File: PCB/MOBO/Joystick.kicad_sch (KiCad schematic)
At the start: 0 parts

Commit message: added full atmega circuit and programming interface
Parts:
- added C4, C5: 22pF, symbol Device:C
- added C6: 100nF, symbol Device:C
- added J107: DTR, TestPoint:TestPoint_Pad_1.5x1.5mm, symbol Connector:Conn_01x01_Male
- added J107: SCK, TestPoint:TestPoint_Pad_1.5x1.5mm, symbol Connector:Conn_01x01_Male
- added J107: TXD, TestPoint:TestPoint_Pad_1.5x1.5mm, symbol Connector:Conn_01x01_Male
- added J107: RXD, TestPoint:TestPoint_Pad_1.5x1.5mm, symbol Connector:Conn_01x01_Male
- added J107: MOSI, TestPoint:TestPoint_Pad_1.5x1.5mm, symbol Connector:Conn_01x01_Male
- added J107: MISO, TestPoint:TestPoint_Pad_1.5x1.5mm, symbol Connector:Conn_01x01_Male
- added R15: 10k, symbol Device:R
- added SW2: Reset_Button, Button_Switch_THT:SW_PUSH_6mm, symbol PCM_SL_Devices:Push_Button
- added U4: ATmega328PB-M, Package_DFN_QFN:QFN-32-1EP_5x5mm_P0.5mm_EP3.1x3.1mm, symbol MCU_Microchip_ATmega:ATmega328PB-M
- added Y1: 116MHz, symbol Device:Crystal
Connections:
- new net: C5.2, U4.8 (XTAL2/PB7), Y1.2
- new net: C6.2, J107.1 (Pin_1)
- new net: C4.1, U4.7 (XTAL1/PB6), Y1.1
- new net 5V_IN: R15.2, U4.18 (AVCC), U4.4 (VCC)
- new net BTN_A: U4.12 (PB0)
- new net BTN_B: U4.13 (PB1)
- new net BTN_DWN: U4.24 (PC1)
- new net BTN_LEFT: U4.25 (PC2)
- new net BTN_LS: U4.14 (PB2)
- new net BTN_RIGHT: U4.26 (PC3)
- new net BTN_RS: U4.32 (PD2)
- new net BTN_UP: U4.23 (PC0)
- new net GND: C4.2, C5.1, SW2.2, U4.21 (GND), U4.33 (GND), U4.5 (GND)
- new net MISO: J107.1 (Pin_1), U4.16 (PB4)
- new net MOSI: J107.1 (Pin_1), U4.15 (PB3)
- new net RESET: C6.1, R15.1, SW2.1, U4.29 (~{RESET}/PC6)
- new net RXD: J107.1 (Pin_1), U4.30 (PD0)
- new net SCK: J107.1 (Pin_1), U4.17 (PB5)
- new net SCL: U4.28 (PC5)
- new net SDA: U4.27 (PC4)
- new net TXD: J107.1 (Pin_1), U4.31 (PD1)
- no-connect marks 0 -> 10

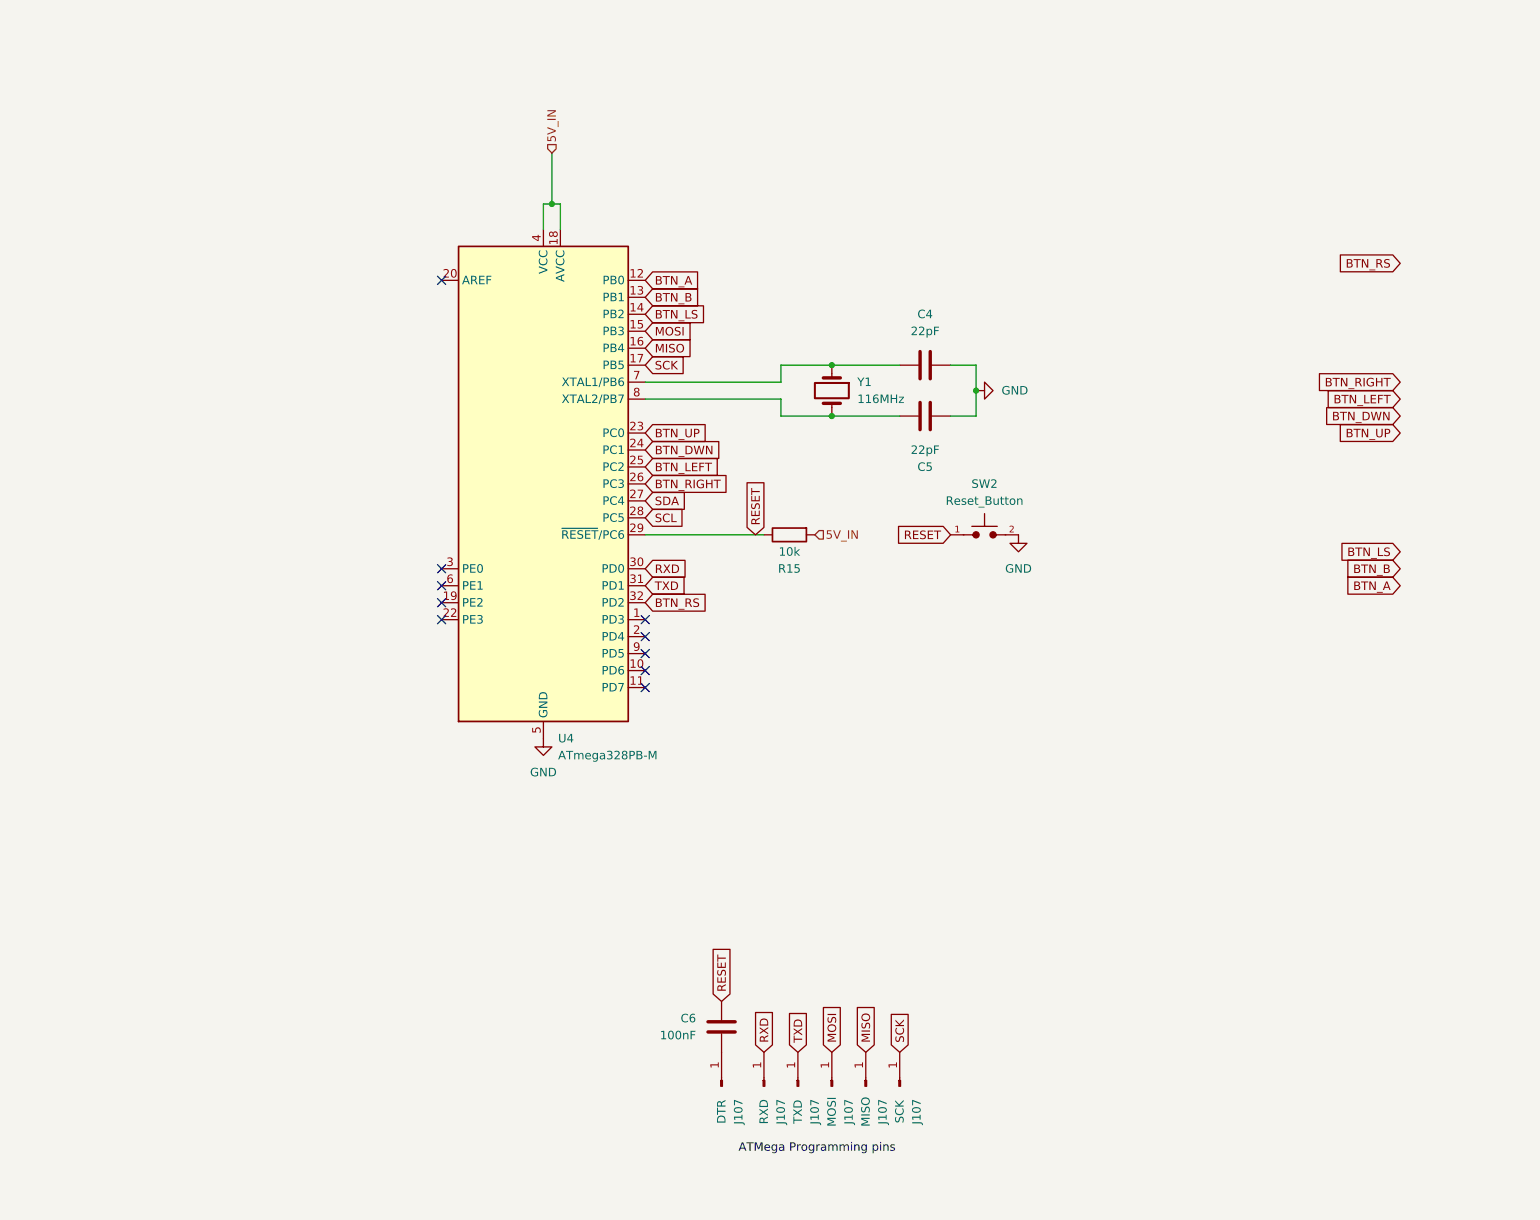
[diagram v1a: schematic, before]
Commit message: added all joystick buttons
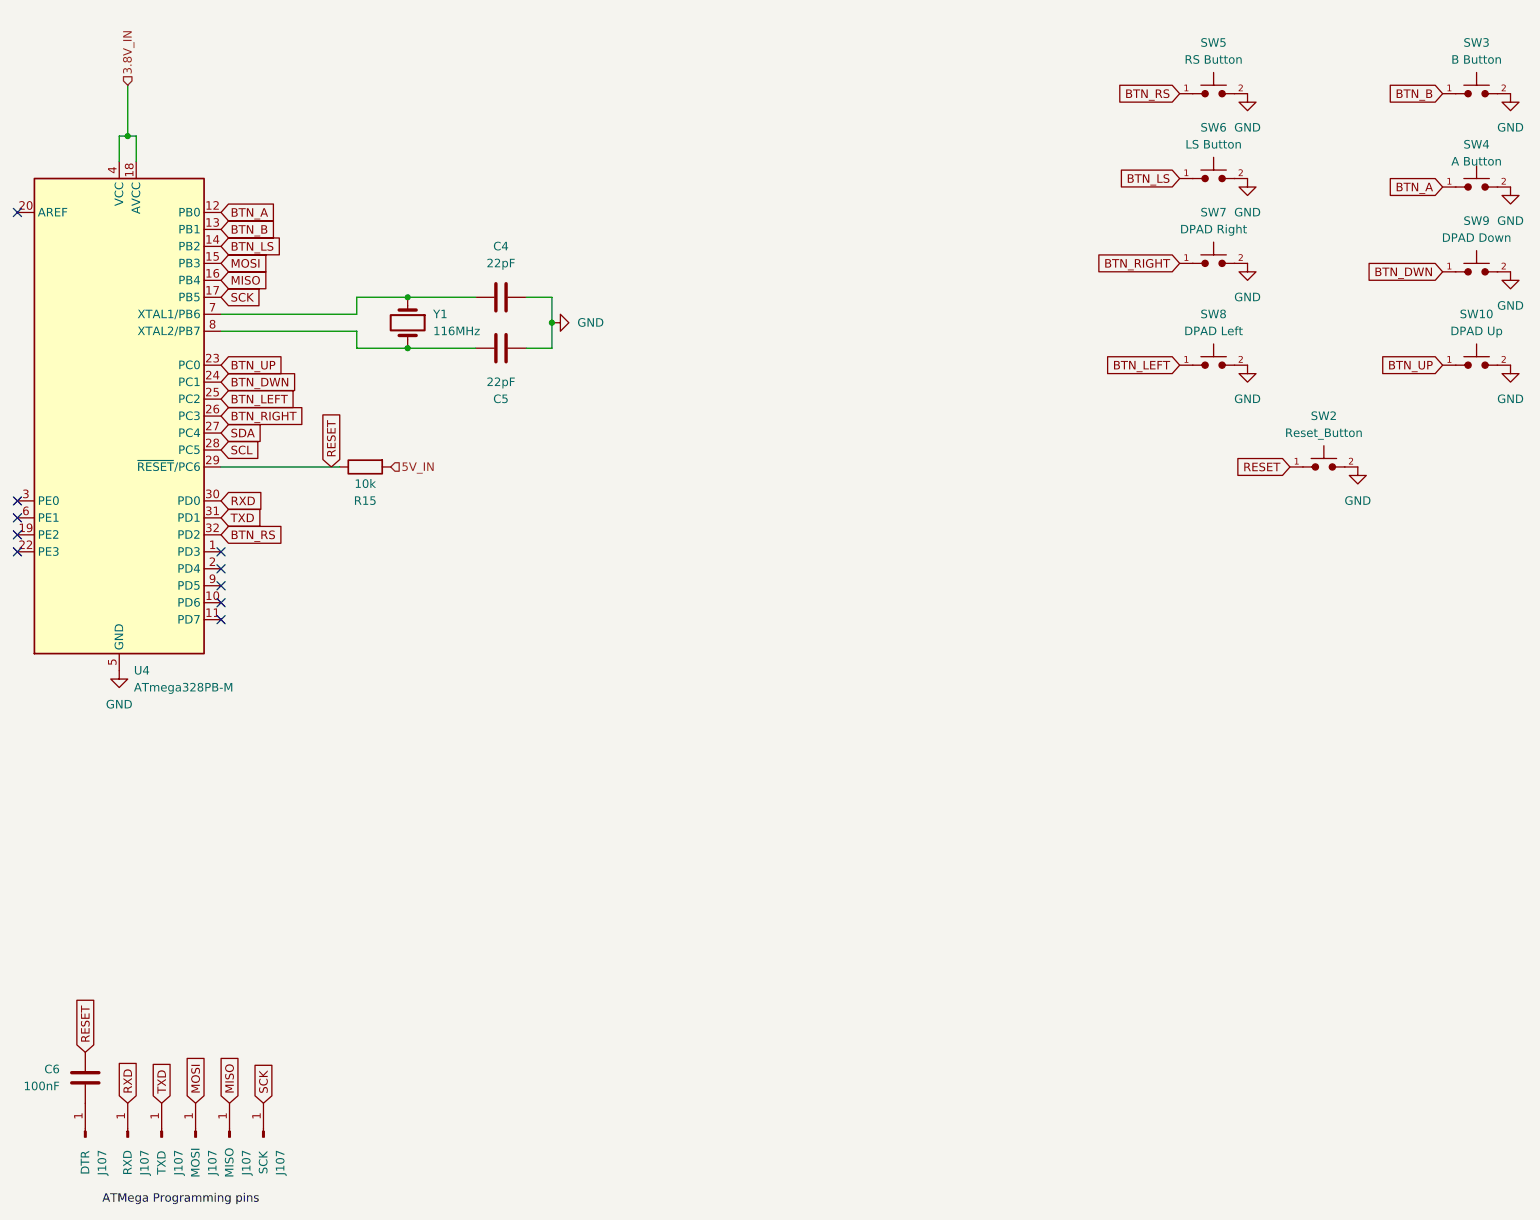
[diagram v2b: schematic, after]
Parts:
- added SW10: DPAD Up, Button_Switch_THT:SW_PUSH_6mm, symbol PCM_SL_Devices:Push_Button
- added SW3: B Button, Button_Switch_THT:SW_PUSH_6mm, symbol PCM_SL_Devices:Push_Button
- added SW4: A Button, Button_Switch_THT:SW_PUSH_6mm, symbol PCM_SL_Devices:Push_Button
- added SW5: RS Button, Button_Switch_THT:SW_PUSH_6mm, symbol PCM_SL_Devices:Push_Button
- added SW6: LS Button, Button_Switch_THT:SW_PUSH_6mm, symbol PCM_SL_Devices:Push_Button
- added SW7: DPAD Right, Button_Switch_THT:SW_PUSH_6mm, symbol PCM_SL_Devices:Push_Button
- added SW8: DPAD Left, Button_Switch_THT:SW_PUSH_6mm, symbol PCM_SL_Devices:Push_Button
- added SW9: DPAD Down, Button_Switch_THT:SW_PUSH_6mm, symbol PCM_SL_Devices:Push_Button
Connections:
- net 5V_IN: no longer U4.18 (AVCC), U4.4 (VCC)
- net BTN_A: now also SW4.1
- net BTN_B: now also SW3.1
- net BTN_DWN: now also SW9.1
- net BTN_LEFT: now also SW8.1
- net BTN_LS: now also SW6.1
- net BTN_RIGHT: now also SW7.1
- net BTN_RS: now also SW5.1
- net BTN_UP: now also SW10.1
- net GND: now also SW10.2, SW3.2, SW4.2, SW5.2, SW6.2, SW7.2, SW8.2, SW9.2
- new net 3.8V_IN: U4.18 (AVCC), U4.4 (VCC)
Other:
- moved on the sheet: C4, C5, C6, J107, R15, SW2, U4, Y1

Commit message: fixed sheet conections and added wiring
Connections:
- net 5V_IN is gone; now on net 3.8V_IN: R15.2
- net ATMEGA_LATCH_S: now reaches U4.1 (PD3)
- no-connect marks 10 -> 9
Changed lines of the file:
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@@
   (no_connect (at 20.32 87.63))
   (no_connect (at 50.8 102.87))
-  (no_connect (at 50.8 95.25))
   (no_connect (at 50.8 97.79))
   (no_connect (at 50.8 100.33))
@@
     )
   )
-  (hierarchical_label "5V_IN" (shape input) (at 76.2 82.55 0) (fields_autoplaced)
-    (effects (font (size 1.27 1.27)) (justify left))
-  )
   (hierarchical_label "3.8V_IN" (shape input) (at 36.83 25.4 90) (fields_autoplaced)
     (effects (font (size 1.27 1.27)) (justify left))
   )
+  (hierarchical_label "3.8V_IN" (shape input) (at 76.2 82.55 0) (fields_autoplaced)
+    (effects (font (size 1.27 1.27)) (justify left))
+  )
+  (hierarchical_label "ATMEGA_LATCH_S" (shape bidirectional) (at 50.8 95.25 0) (fields_autoplaced)
+    (effects (font (size 1.27 1.27)) (justify left))
+  )

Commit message: added connector
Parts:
- renumbered C6 to C301, C4 to C302, C5 to C303, R15 to R301, SW5 to SW301, SW6 to SW302, SW7 to SW303, SW8 to SW304, SW2 to SW305, SW3 to SW306, SW4 to SW307, SW9 to SW308, SW10 to SW309, U4 to U301, Y1 to Y301

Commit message: schematic cleanup Added:  - Power flags  - Fixed loose connections
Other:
- note added: "ATMega Programming Interface"
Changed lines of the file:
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@@
     (stroke (width 0) (type default))
   )
-  (label "ATMega Programming pins" (at 33.02 193.04 0) (fields_autoplaced)
+  (text "ATMega Programming Interface\n" (at 30.48 191.77 0)
     (effects (font (size 1.27 1.27)) (justify left bottom))
   )

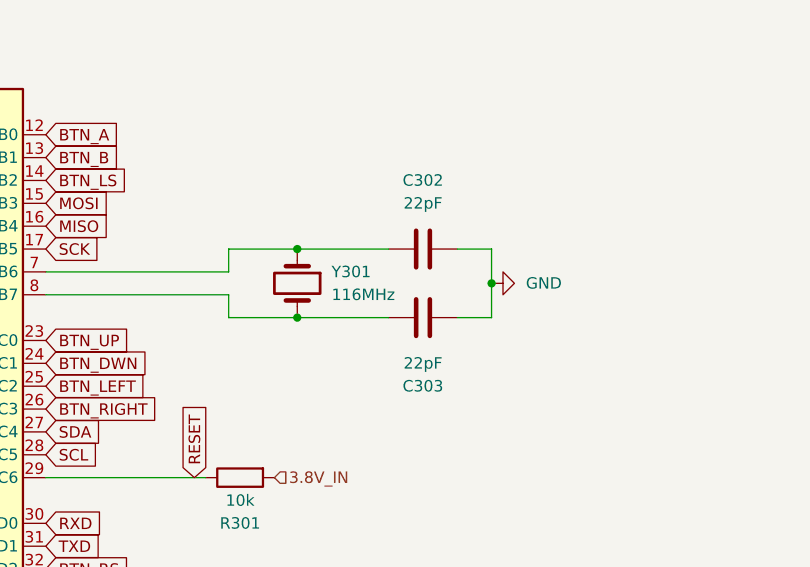
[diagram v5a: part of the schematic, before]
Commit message: added all footprints
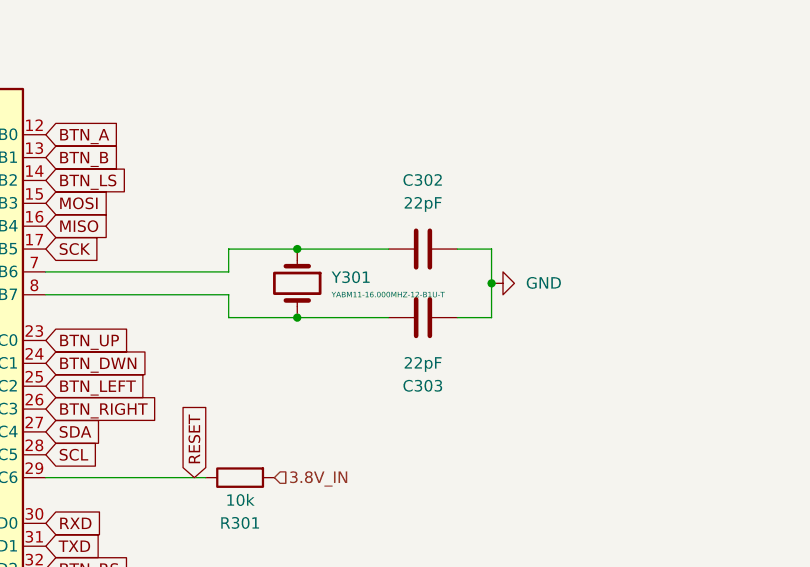
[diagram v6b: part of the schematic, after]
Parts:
- C301, C302, C303: footprint (none) -> Capacitor_SMD:C_0805_2012Metric
- R301: footprint (none) -> Resistor_SMD:R_0805_2012Metric
- Y301: value 116MHz -> YABM11-16.000MHZ-12-B1U-T; footprint (none) -> Crystal:Crystal_SMD_2016-4Pin_2.0x1.6mm
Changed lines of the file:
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@@
       (effects (font (size 1.27 1.27)))
     )
-    (property "Footprint" "" (at 88.9 63.8048 0)
+    (property "Footprint" "Capacitor_SMD:C_0805_2012Metric" (at 88.9 63.8048 0)
       (effects (font (size 1.27 1.27)) hide)
     )
@@
       (effects (font (size 1.27 1.27)))
     )
-    (property "Footprint" "" (at 96.52 56.1848 0)
+    (property "Footprint" "Capacitor_SMD:C_0805_2012Metric" (at 96.52 56.1848 0)
       (effects (font (size 1.27 1.27)) hide)
     )
@@
   (symbol (lib_id "Device:Crystal") (at 78.74 60.96 270) (unit 1)
     (in_bom yes) (on_board yes) (dnp no) (fields_autoplaced)
-    (property "Reference" "Y301" (at 82.55 59.69 90)
+    (property "Reference" "Y301" (at 82.55 60.325 90)
       (effects (font (size 1.27 1.27)) (justify left))
     )
-    (property "Value" "116MHz" (at 82.55 62.23 90)
-      (effects (font (size 1.27 1.27)) (justify left))
-    )
-    (property "Footprint" "" (at 78.74 60.96 0)
+    (property "Value" "YABM11-16.000MHZ-12-B1U-T" (at 82.55 62.23 90)
+      (effects (font (size 0.6 0.6)) (justify left))
+    )
+    (property "Footprint" "Crystal:Crystal_SMD_2016-4Pin_2.0x1.6mm" (at 78.74 60.96 0)
       (effects (font (size 1.27 1.27)) hide)
     )
@@
       (effects (font (size 1.27 1.27)))
     )
-    (property "Footprint" "" (at 72.39 80.772 90)
+    (property "Footprint" "Resistor_SMD:R_0805_2012Metric" (at 72.39 80.772 90)
       (effects (font (size 1.27 1.27)) hide)
     )
@@
       (effects (font (size 1.27 1.27)) (justify right))
     )
-    (property "Footprint" "" (at 31.4452 177.8 0)
-      (effects (font (size 1.27 1.27)) hide)
-    )
+    (property "Footprint" "Capacitor_SMD:C_0805_2012Metric" (at 31.4452 177.8 0)
+      (effects (font (size 1.27 1.27)) hide)
+    )
